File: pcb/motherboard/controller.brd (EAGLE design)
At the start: 73.7 x 76.2 mm, 103 parts, among them J1 SNG-2MM-HEADER-04-V, J2 DL-1.25MM-HEADER-20, J3 MICRO_SD, J4 SNG-100-HEADER-01-HDR-V, J5 7498011122R, J6 USB_A, J7 DL-1.25MM-HEADER-10, J8 CUI-PJ-013C, J9 SNG-100-HEADER-05-HDR-V, Q1 12MHz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

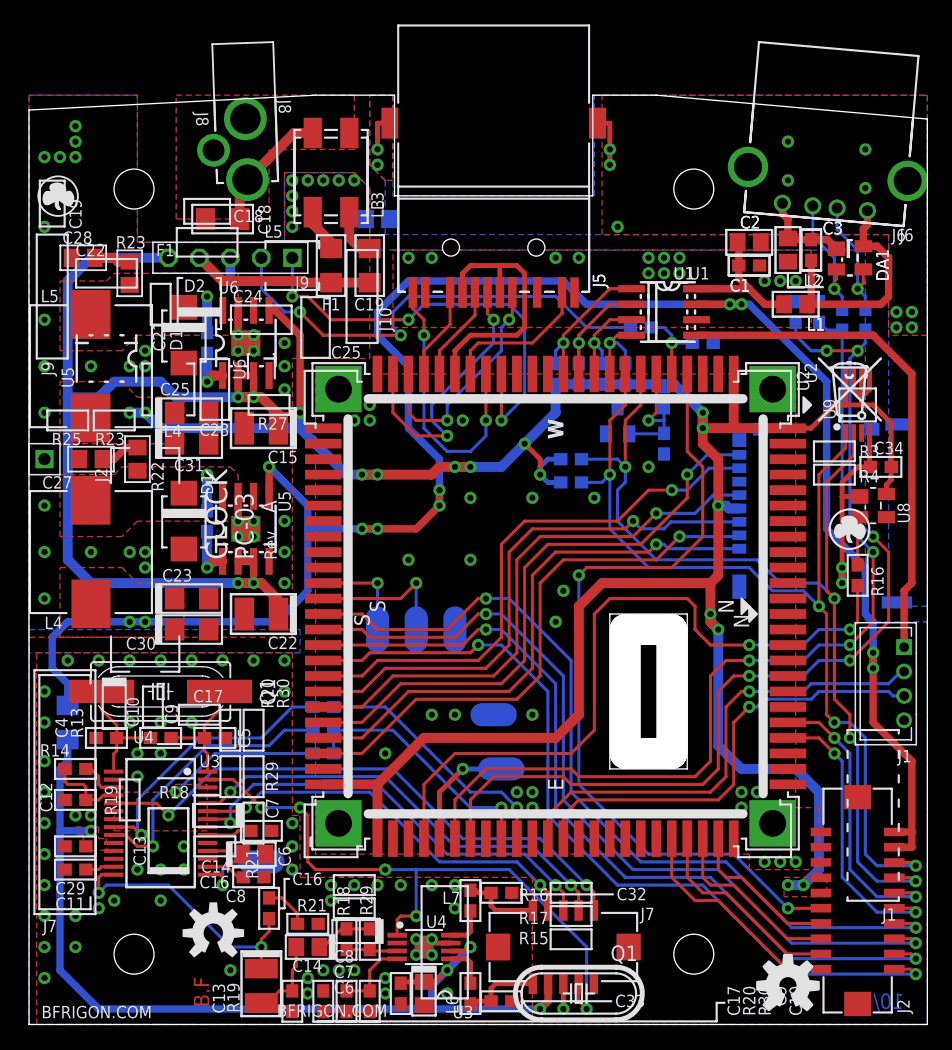
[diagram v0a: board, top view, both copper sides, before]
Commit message: Swapped USBC and USBB, USBC will be used for the PCM2704
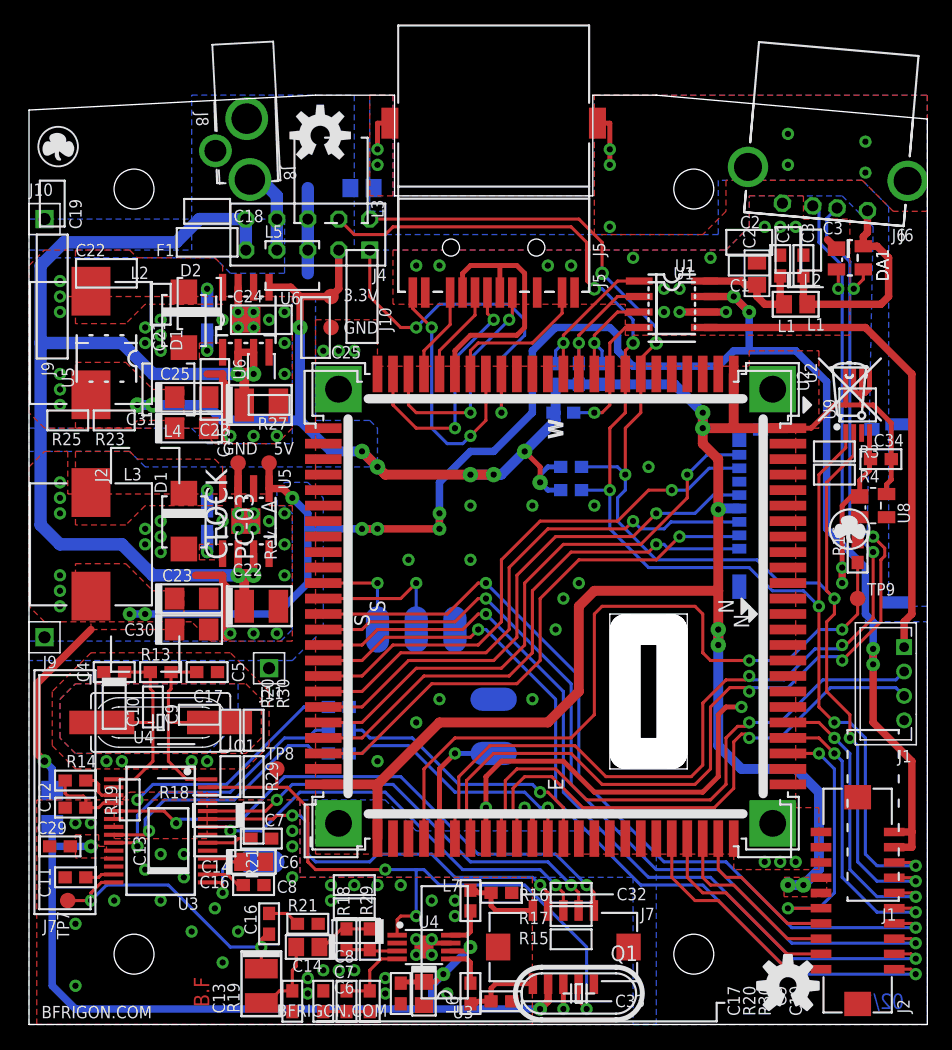
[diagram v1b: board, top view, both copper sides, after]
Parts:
- removed C18, C19: 10uF 25V, Passive:SMD_1206
- removed C26: 100nF, Passive:SMD_0603
- removed C27, C28: 1nF, Passive:SMD_0805
- removed F1: 3A, Passive:SMD_1206
- removed L4, L5: 22uH, Passive:IND-10X10
- removed R10, R9: 22, Passive:SMD_0603
- removed R11, R12: 15k, Passive:SMD_0603
- removed R22, R23: 1 (1%), Passive:SMD_0805
- removed R24: 12M (1%), Passive:SMD_0603
- removed R26: 4.7M (1%), Passive:SMD_0603
- removed R28: 1k, Passive:SMD_0603
- removed U7: LM4040D25IDBZR, Passive:SOT23
- added J10, J11: SNG-100-HEADER-01-HDR-V, Connectors:HDR_M_1
- added TP3, TP4, TP5, TP6, TP7, TP8, TP9: (no value), Misc:TP_050
- J4: value SNG-100-HEADER-01-HDR-V -> (none); device Connectors:HDR_M_1 -> Connectors:534206-5
- J6: device Connectors:292303-7 -> Connectors:292303-1
- J9: value SNG-100-HEADER-05-HDR-V -> SNG-100-HEADER-01-HDR-V; device Connectors:HDR_M_5 -> Connectors:HDR_M_1
- L2: value 1A -> 10uH; device Passive:SMD_0805 -> Passive:IND-10X10
- L3: value ACM7060701-2PL-TL01 -> 10uH; device Passive:ACM7060 -> Passive:IND-10X10
- R17: value (none) -> 0
- moved U$1 66.0 mm to (23.9, 72.9)
- moved U$3 59.7 mm to (66.0, 54.6), turned to 0 degrees
- moved L2 57.7 mm to (5.08, 55.9), turned to 270 degrees
- moved J9 37.2 mm to (1.27, 31.8), turned to 0 degrees
- moved L3 36.3 mm to (5.08, 39.4)
- moved J4 28.4 mm to (22.9, 64.8)
- moved R17 7.10 mm to (1.91, 17.8)
- moved R6 5.99 mm to (43.8, 50.2), turned to 0 degrees
- moved C4 5.43 mm to (6.99, 28.9)
- moved C5 5.43 mm to (14.6, 28.9)
- moved R13 5.40 mm to (10.8, 28.9)
- moved U$4 4.06 mm to (2.41, 72.0)
- moved R1 4.02 mm to (25.4, 22.2)
- moved R15 4.02 mm to (25.4, 26.0)
- moved C20 2.84 mm to (27.3, 68.6)
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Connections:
- net N$11 renamed BST_5V
- net N$36 renamed BST_3.3V
- removed net IN_GND: C18.2, J8.2, J8.3, L3.IA
- removed net N$2: C27.1, R22.1
- removed net N$3: C28.1, R23.1
- removed net N$32: F1.1, L3.OB
- removed net N$4: C18.1, J8.1, L3.IB
- removed net N$6: C3.2, DA1.1, J6.4, L2.2
- removed net N$7: DA1.3, J6.2, R9.2
- removed net N$8: DA1.2, J6.3, R10.2
- removed net V_AUX_MON: J9.2, R24.2
- removed net V_IN: C15.+, C22.+, J9.5, U5.2, U5.3, U6.2, U6.3
- removed net V_MAIN: C19.1, F1.2, J9.4
- new net 9V: C15.+, C22.+, J4.10, J4.9, U5.2, U5.3, U6.2, U6.3
- new net N$23: J4.7, J4.8, J8.1
- new net PC20/PWM2: J2.11, U2.N22
- net 3.3V: now also J4.3, L2.2, TP5.1; no longer L5.2, R28.2
- net 5V: now also L3.2, TP3.1; no longer L4.2
- net AD0: no longer R24.1, R26.2
- net AD1: no longer J2.11
- net DAC_SHDN: now also TP8.1
- net GND: now also C3.2, DA1.1, J4.5, J4.6, J6.4, J8.2, J8.3, TP4.1, TP6.1; no longer C19.2, C26.2, C27.2, C28.2, J4.1, J9.3, L2.1, L3.OA, R11.1, R12.1, R26.1, U7.2
- net NRST: now also TP9.1
- net SCL0: now also J4.2
- net SDA0: now also J4.4
- net SW_3.3: now also L2.1; no longer L5.1, R23.2
- net SW_5V: now also L3.1; no longer L4.1, R22.2
- net USBA_D+: now also DA1.2, J6.3; no longer R10.1, R12.2
- net USBA_D-: now also DA1.3, J6.2; no longer R11.2, R9.1
- net USBB_D+: now also J1.2; no longer R15.1, R2.1
- net USBB_D-: now also J1.3; no longer R1.1
- net USBC_D+: now also R15.1, R2.1; no longer J1.3
- net USBC_D-: now also R1.1; no longer J1.2
- net VOUTL: now also TP7.1
- net VREF: no longer C26.1, R28.1, U7.1
- net V_AUX_ON: now also J4.1; no longer J9.1
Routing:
- net 9V: track 0.00 -> 96.9 mm, vias 0 -> 4
- net V_IN: track 82.1 -> 0.00 mm, vias 4 -> 0
- net AD1: track 66.6 -> 0.00 mm, vias 2 -> 0
- net GND: track 29.4 -> 86.2 mm, vias 143 -> 126
- net V_AUX_MON: track 38.8 -> 0.00 mm, vias 2 -> 0
- net SDA0: track 79.7 -> 114.1 mm, vias 4 -> 6
- net SCL0: track 81.6 -> 115.1 mm, vias 4 -> 6
- net USBB_D+: track 20.8 -> 45.6 mm
- net USBB_D-: track 21.0 -> 44.6 mm
- net PC20/PWM2: track 0.00 -> 21.6 mm, vias 0 -> 2
- net USBC_D-: track 39.3 -> 21.2 mm
- net V_MAIN: track 14.8 -> 0.00 mm
- net USBC_D+: track 37.2 -> 24.6 mm
- net USBA_D+: track 75.3 -> 87.8 mm, vias 3 -> 4
- net N$8: track 11.1 -> 0.00 mm, vias 1 -> 0
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- added copper zone on layer 1, net BST_3.3V
- added copper zone on layer 1, net BST_5V
- added copper zone on layer 16, net N$2
- added copper zone on layer 16, net N$22
- added copper zone on layer 1, net N$30
- added copper zone on layer 16, net N$4
- removed copper zone on layer 1, net IN_GND
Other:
- board text added: "3.3V"
- board text added: "5V"

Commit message: Switched motherboard (PC-03) to 4 layers design
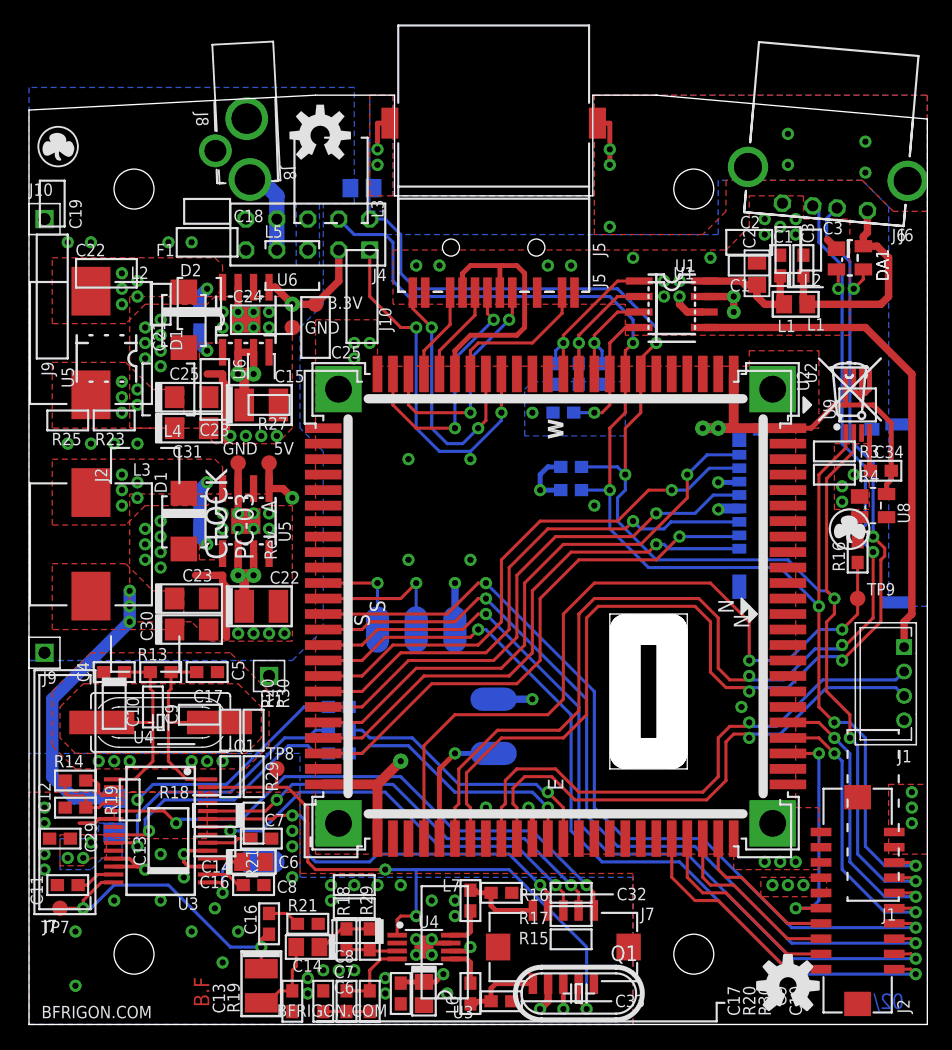
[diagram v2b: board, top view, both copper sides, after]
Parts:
- moved R17 5.12 mm to (6.99, 17.1)
- moved TP6 3.18 mm to (21.6, 57.1)
- moved TP5 1.42 mm to (23.5, 59.1)
- moved J9 1.27 mm to (1.27, 30.5)
- moved C34 0.95 mm to (69.8, 45.4)
- moved C11 0.90 mm to (3.17, 11.4)
- moved TP7 0.90 mm to (2.54, 9.53)
- moved C21 0.90 mm to (14.0, 41.9)
- moved J11 0.64 mm to (19.7, 28.6)
- moved C24 0.63 mm to (14.0, 57.8)
- moved C29 0.63 mm to (2.54, 15.2)
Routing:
- net 3.3V: track 220.2 -> 121.8 mm, vias 16 -> 15
- net 5V_AUD: track 71.5 -> 7.95 mm, vias 4 -> 6
- net 9V: track 96.9 -> 64.4 mm
- net GND: track 86.2 -> 55.6 mm, vias 126 -> 127
- net USBA_D+: track 87.8 -> 95.9 mm
- net USBA_D-: track 88.6 -> 96.3 mm
- net PC20/PWM2: track 21.6 -> 18.9 mm
- net NRST: track 61.1 -> 63.1 mm
- net 5V: track 158.2 -> 156.4 mm, vias 12 -> 9
- net VOUTL: track 24.9 -> 26.7 mm
- net V_AUX_ON: track 30.5 -> 29.6 mm
- net SDA0: track 114.1 -> 113.2 mm, vias 6 -> 5
- net N$14: track 2.38 -> 3.28 mm
- net USBB_D-: track 44.6 -> 43.7 mm
- net SPCK: track 68.1 -> 68.8 mm
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- added copper zone on layer 16, net 3.3V
- added copper zone on layer 3, net 3.3V
- added copper zone on layer 3, net 5V
- added copper zone on layer 16, net 5V_AUD
- added copper zone on layer 3, net 5V_AUD
- added copper zone on layer 3, net 9V
- added copper zone on layer 2, net GND
- added copper zone on layer 2, net N$2
- added copper zone on layer 2, net N$3
- added copper zone on layer 2, net N$4
- added copper zone on layer 3, net SW_3.3
- added copper zone on layer 3, net SW_5V
- removed copper zone on layer 16, net N$10
- removed copper zone on layer 16, net N$2
- removed copper zone on layer 16, net N$22
- removed copper zone on layer 16, net N$4
